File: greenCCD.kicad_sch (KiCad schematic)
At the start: 27 parts, among them J1 USB_C_Receptacle, J2 USB_C_Receptacle_USB2.0_14P, U1 TPD4EUSB30DQAR, U2 USB2422/MJ, Y1 24MHz

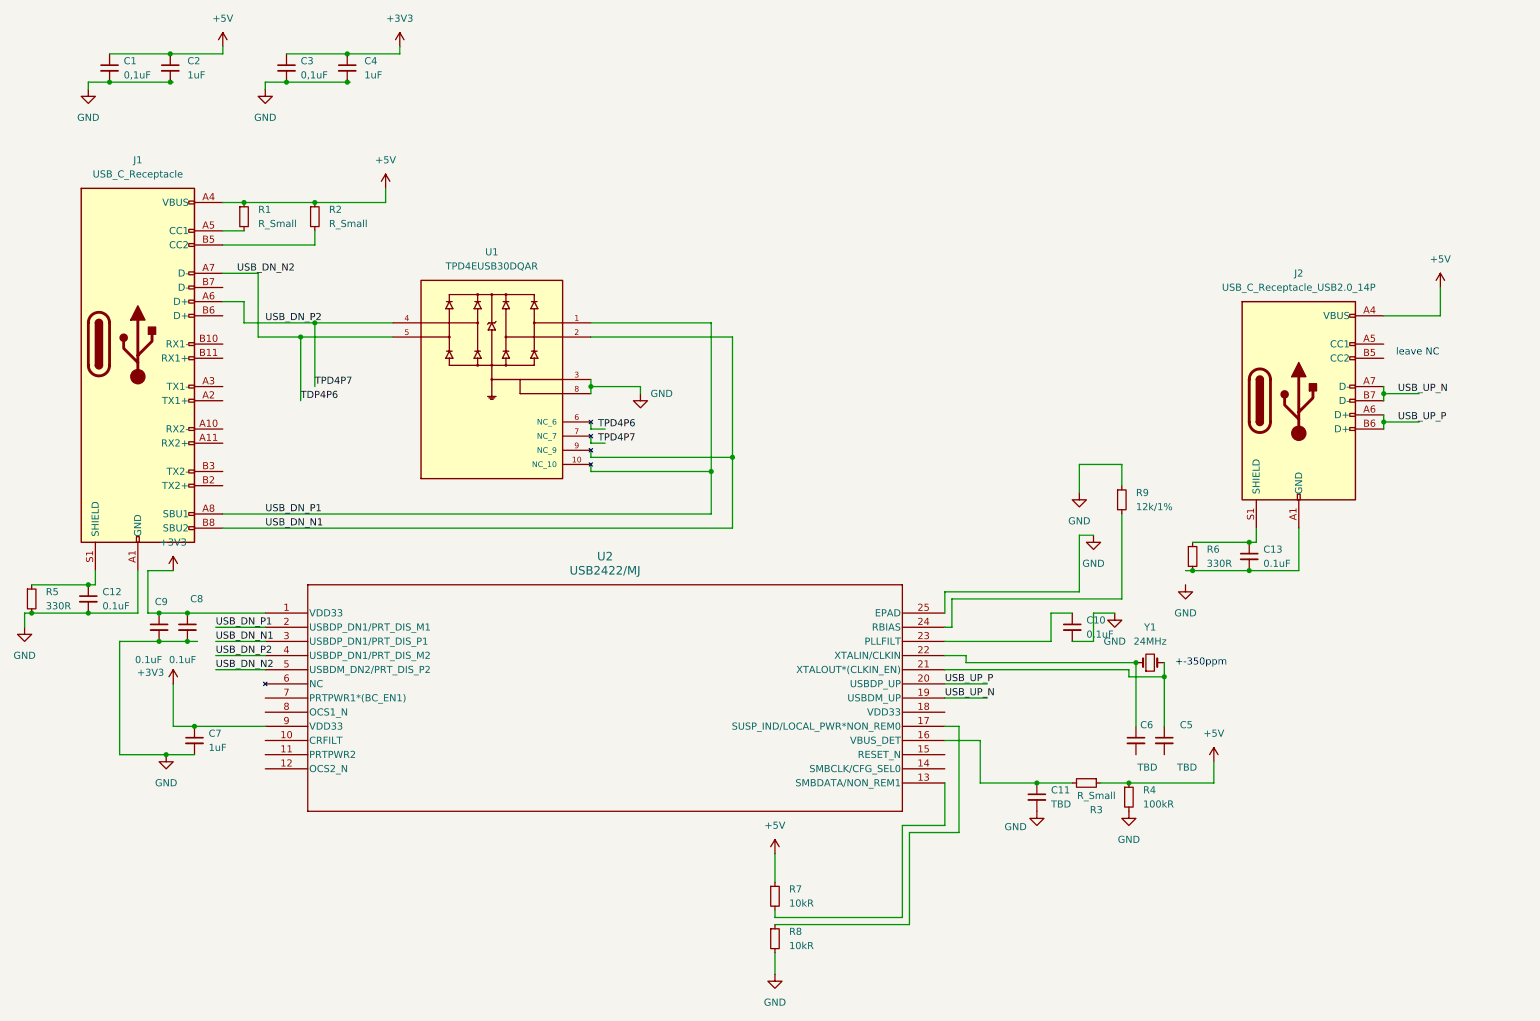
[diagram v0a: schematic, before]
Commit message: add voltage regulator
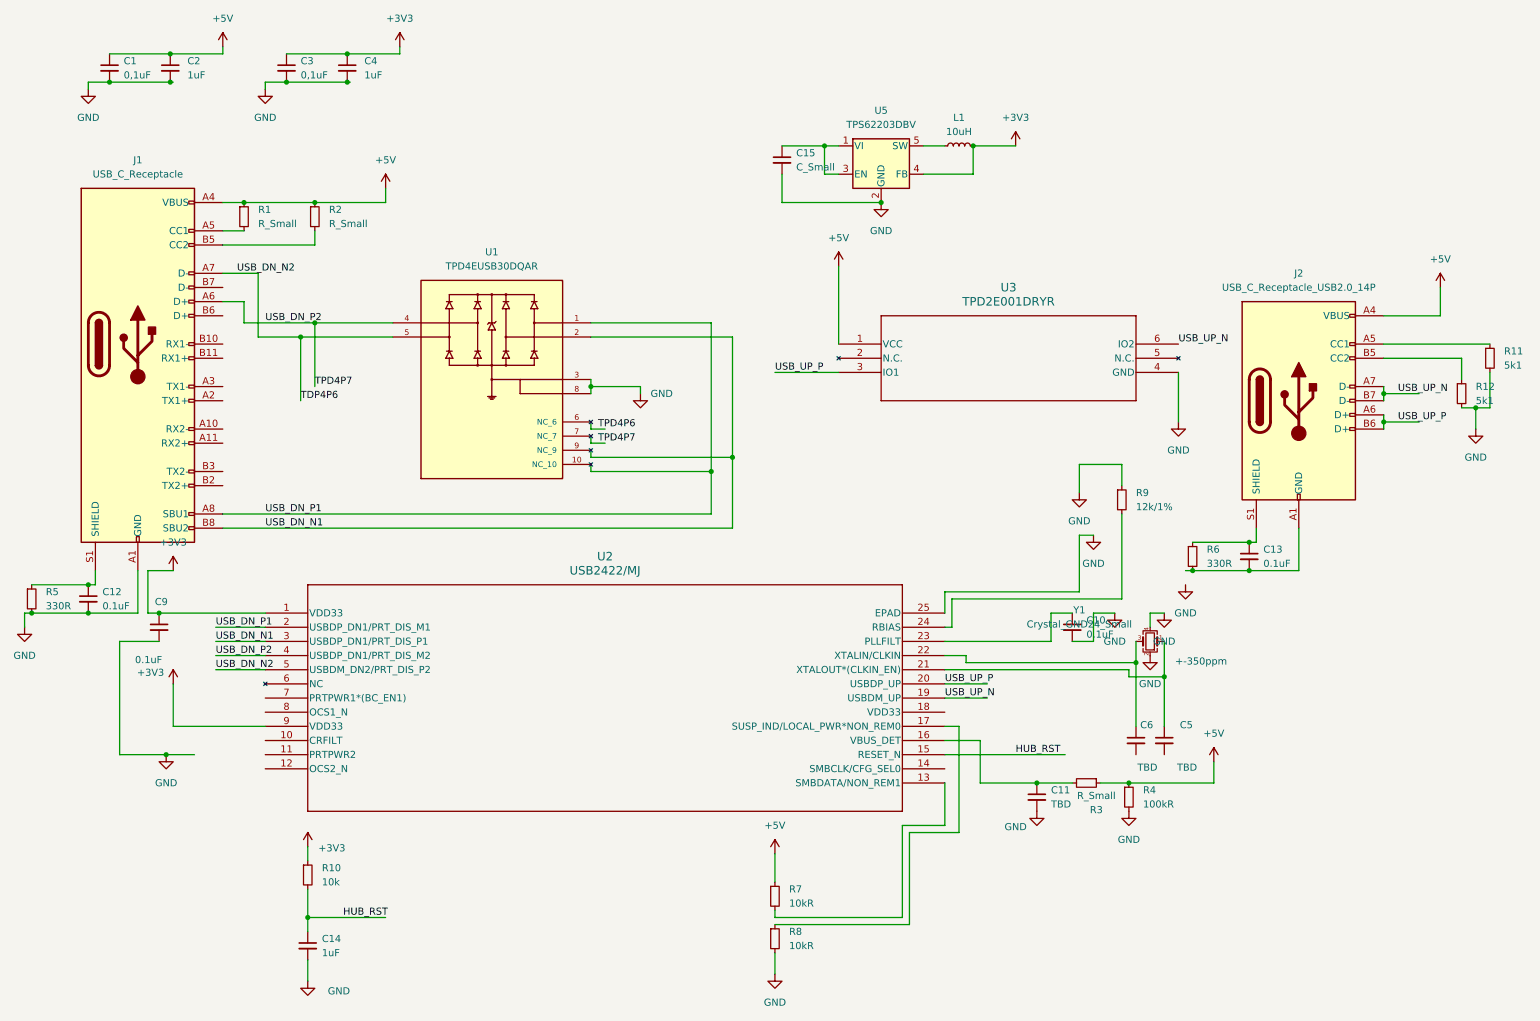
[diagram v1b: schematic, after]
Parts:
- removed C7: 1uF, symbol Device:C_Small
- removed C8: 0.1uF, symbol Device:C_Small
- removed Y1: 24MHz, symbol Device:Crystal_Small
- added C14: 1uF, Capacitor_SMD:C_0402_1005Metric, symbol Device:C_Small
- added C15: C_Small, Capacitor_SMD:C_0402_1005Metric, symbol Device:C_Small
- added L1: 10uH, Inductor_SMD:L_0402_1005Metric, symbol Device:L_Small
- added R10: 10k, Resistor_SMD:R_0402_1005Metric, symbol Device:R_Small
- added R11, R12: 5k1, Resistor_SMD:R_0402_1005Metric, symbol Device:R_Small
- added U3: TPD2E001DRYR, footprints:DRY6, symbol 2024-08-27_14-38-34:TPD2E001DRYR
- added U5: TPS62203DBV, Package_TO_SOT_SMD:SOT-23-5, symbol Regulator_Switching:TPS62203DBV
- added Y1: Crystal_GND24_Small, Crystal:Crystal_SMD_3225-4Pin_3.2x2.5mm, symbol Device:Crystal_GND24_Small
- C1, C10, C11, C12, C13, C2, C3, C4, C5, C6, C9: footprint (none) -> Capacitor_SMD:C_0402_1005Metric
- J1: footprint (none) -> Connector_USB:USB_C_Plug_JAE_DX07P024AJ1
- J2: footprint (none) -> Connector_USB:USB_C_Receptacle_Amphenol_12401548E4-2A
- R1, R2, R3, R4, R5, R6, R7, R8, R9: footprint (none) -> Resistor_SMD:R_0402_1005Metric
- U1: footprint TPD4EUSB30DQAR:IC_TPD4EUSB30DQAR -> footprints:DQA10
- U2: footprint SQFN24_4X4MC_MCH -> footprints:SQFN24_4X4MC_MCH
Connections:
- net +3V3: now also L1.2, R10.1, U5.4 (FB)
- net +5V: now also U3.1 (VCC)
- net GND: now also C14.2, C15.2, R11.2, R12.2, U3.4 (GND), U5.2 (GND), Y1.2, Y1.4
- net USB_UP_N: now also U3.6 (IO2)
- net USB_UP_P: now also U3.3 (IO1)
- net at J2.A5 (CC1): now also R11.1
- net at J2.B5 (CC2): now also R12.1
- net at C5.1, U2.21 (XTALOUT*(CLKIN_EN)): now also Y1.1
- net HUB_RST: now reaches U2.15 (RESET_N)
- net HUB_RST: now also C14.1, R10.2
- net at C6.1, U2.22 (XTALIN/CLKIN): now also Y1.3
- new net: C15.1, U5.1 (VI), U5.3 (EN)
- new net: L1.1, U5.5 (SW)
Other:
- note removed: "leave NC"
